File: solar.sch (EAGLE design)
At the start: 13 parts, among them J1 POWERPOLE_POWER10AWG, J2 POWERPOLE_POWER10AWG, J3 POWERPOLE_POWER10AWG, J4 POWERPOLE_POWER10AWG, J5 POWERPOLE_POWER10AWG

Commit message: Uses PCB mount instead of cable for power pole
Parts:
- J1, J2, J3, J4, J5: value POWERPOLE_POWER10AWG -> POWERPOLE_POWER25A; device powerpoles:POWERPOLE_POWER10AWG -> powerpoles:POWERPOLE_POWER25A
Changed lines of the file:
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@@
 </classes>
 <parts>
-<part name="J1" library="powerpoles" deviceset="POWERPOLE_POWER" device="10AWG"/>
-<part name="J2" library="powerpoles" deviceset="POWERPOLE_POWER" device="10AWG"/>
-<part name="J3" library="powerpoles" deviceset="POWERPOLE_POWER" device="10AWG"/>
-<part name="J4" library="powerpoles" deviceset="POWERPOLE_POWER" device="10AWG"/>
-<part name="J5" library="powerpoles" deviceset="POWERPOLE_POWER" device="10AWG"/>
+<part name="J1" library="powerpoles" deviceset="POWERPOLE_POWER" device="25A" value="POWERPOLE_POWER25A"/>
+<part name="J2" library="powerpoles" deviceset="POWERPOLE_POWER" device="25A" value="POWERPOLE_POWER25A"/>
+<part name="J3" library="powerpoles" deviceset="POWERPOLE_POWER" device="25A" value="POWERPOLE_POWER25A"/>
+<part name="J4" library="powerpoles" deviceset="POWERPOLE_POWER" device="25A" value="POWERPOLE_POWER25A"/>
+<part name="J5" library="powerpoles" deviceset="POWERPOLE_POWER" device="25A" value="POWERPOLE_POWER25A"/>
 <part name="GND1" library="glacsweb" deviceset="GND" device=""/>
 <part name="GND2" library="glacsweb" deviceset="GND" device=""/>

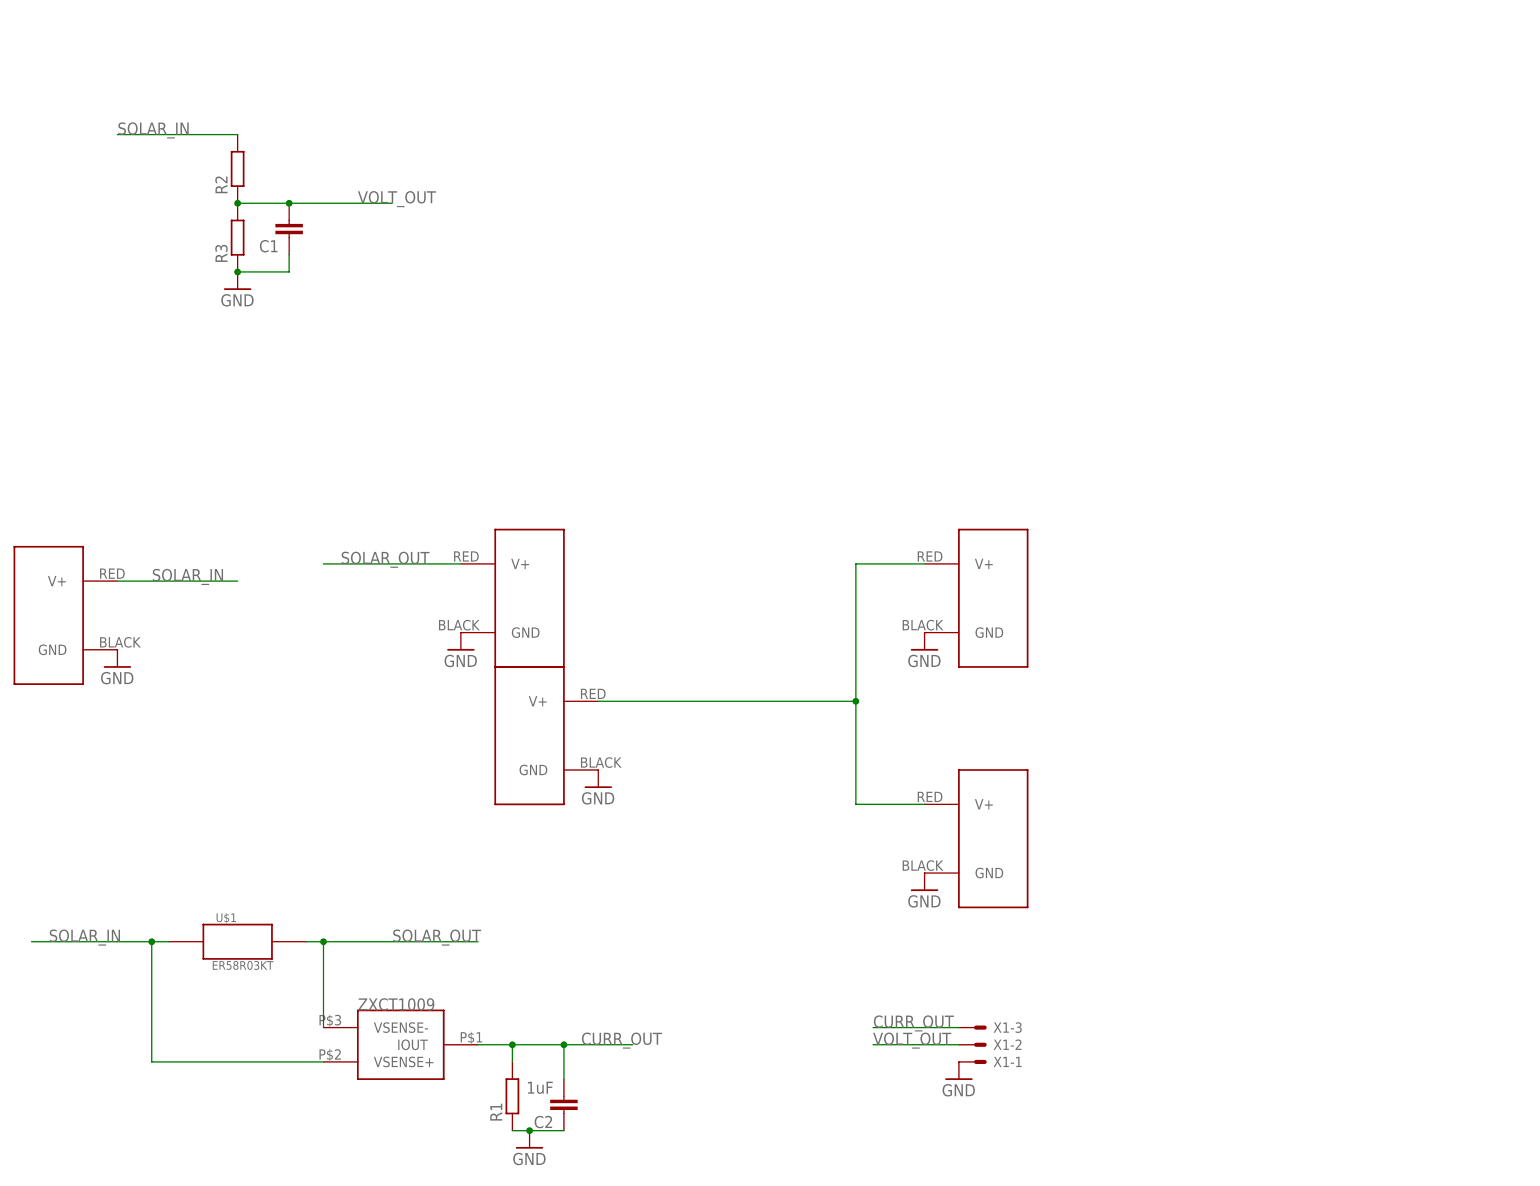
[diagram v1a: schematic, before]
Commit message: now uses smaller frame
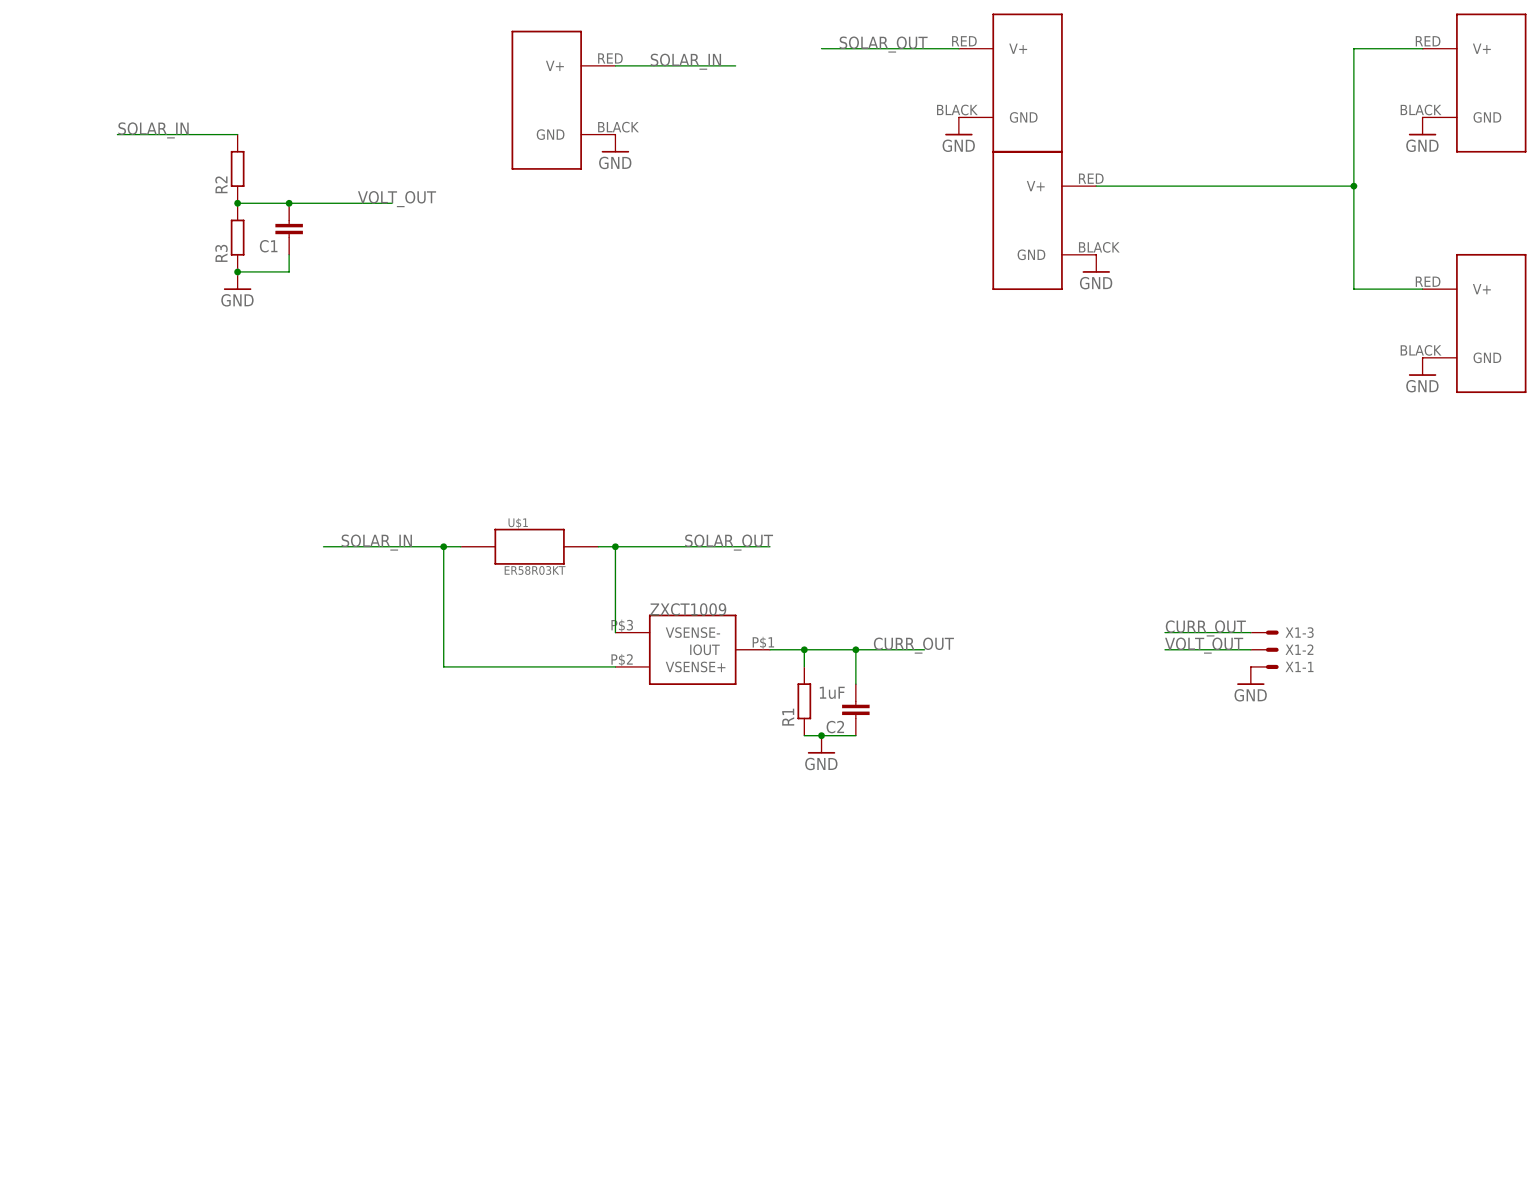
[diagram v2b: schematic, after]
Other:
- moved on the sheet: C2, R1, U$1, X1-1, X1-2, X1-3
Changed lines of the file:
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@@
 <part name="GND8" library="glacsweb" deviceset="GND" device=""/>
 <part name="GND7" library="glacsweb" deviceset="GND" device=""/>
+<part name="FRAME1" library="frames" deviceset="A4L-LOC" device=""/>
 </parts>
 <sheets>
@@
 </plain>
 <instances>
-<instance part="J1" gate="G$1" x="10.16" y="73.66" rot="MR0"/>
-<instance part="J2" gate="G$1" x="81.28" y="55.88" rot="MR0"/>
-<instance part="J3" gate="G$1" x="81.28" y="76.2"/>
-<instance part="J4" gate="G$1" x="149.86" y="76.2"/>
-<instance part="J5" gate="G$1" x="149.86" y="40.64"/>
-<instance part="GND1" gate="1" x="20.32" y="66.04"/>
-<instance part="GND2" gate="1" x="71.12" y="68.58"/>
-<instance part="GND3" gate="1" x="91.44" y="48.26"/>
-<instance part="GND4" gate="1" x="139.7" y="68.58"/>
-<instance part="GND5" gate="1" x="139.7" y="33.02"/>
-<instance part="U$1" gate="G$1" x="38.1" y="25.4"/>
-<instance part="U$2" gate="G$1" x="63.5" y="10.16"/>
-<instance part="R1" gate="G$1" x="78.74" y="2.54" rot="R90"/>
+<instance part="J1" gate="G$1" x="83.82" y="149.86" rot="MR0"/>
+<instance part="J2" gate="G$1" x="154.94" y="132.08" rot="MR0"/>
+<instance part="J3" gate="G$1" x="154.94" y="152.4"/>
+<instance part="J4" gate="G$1" x="223.52" y="152.4"/>
+<instance part="J5" gate="G$1" x="223.52" y="116.84"/>
+<instance part="GND1" gate="1" x="93.98" y="142.24"/>
+<instance part="GND2" gate="1" x="144.78" y="144.78"/>
+<instance part="GND3" gate="1" x="165.1" y="124.46"/>
+<instance part="GND4" gate="1" x="213.36" y="144.78"/>
+<instance part="GND5" gate="1" x="213.36" y="109.22"/>
+<instance part="U$1" gate="G$1" x="81.28" y="83.82"/>
+<instance part="U$2" gate="G$1" x="106.68" y="68.58"/>
+<instance part="R1" gate="G$1" x="121.92" y="60.96" rot="R90"/>
 <instance part="R2" gate="G$1" x="38.1" y="139.7" rot="R90"/>
 <instance part="R3" gate="G$1" x="38.1" y="129.54" rot="R90"/>
 <instance part="C1" gate="G$1" x="45.72" y="129.54" rot="R180"/>
-<instance part="C2" gate="G$1" x="86.36" y="0" rot="R180"/>
-<instance part="X1" gate="-1" x="147.32" y="7.62"/>
-<instance part="X1" gate="-2" x="147.32" y="10.16"/>
-<instance part="X1" gate="-3" x="147.32" y="12.7"/>
-<instance part="GND6" gate="1" x="81.28" y="-5.08"/>
+<instance part="C2" gate="G$1" x="129.54" y="58.42" rot="R180"/>
+<instance part="X1" gate="-1" x="190.5" y="66.04"/>
+<instance part="X1" gate="-2" x="190.5" y="68.58"/>
+<instance part="X1" gate="-3" x="190.5" y="71.12"/>
+<instance part="GND6" gate="1" x="124.46" y="53.34"/>
 <instance part="GND8" gate="1" x="38.1" y="121.92"/>
-<instance part="GND7" gate="1" x="144.78" y="5.08"/>
+<instance part="GND7" gate="1" x="187.96" y="63.5"/>
+<instance part="FRAME1" gate="G$1" x="0" y="0"/>
 </instances>
 <busses>
@@
 <pinref part="R1" gate="G$1" pin="1"/>
 <pinref part="C2" gate="G$1" pin="1"/>
-<wire x1="78.74" y1="-2.54" x2="81.28" y2="-2.54" width="0.1524" layer="91"/>
+<wire x1="121.92" y1="55.88" x2="124.46" y2="55.88" width="0.1524" layer="91"/>
 <pinref part="GND6" gate="1" pin="GND"/>
-<wire x1="81.28" y1="-2.54" x2="86.36" y2="-2.54" width="0.1524" layer="91"/>
-<junction x="81.28" y="-2.54"/>
+<wire x1="124.46" y1="55.88" x2="129.54" y2="55.88" width="0.1524" layer="91"/>
+<junction x="124.46" y="55.88"/>
 </segment>
 <segment>
@@
 <segment>
 <pinref part="J2" gate="G$1" pin="V+"/>
-<wire x1="91.44" y1="60.96" x2="129.54" y2="60.96" width="0.1524" layer="91"/>
-<wire x1="129.54" y1="60.96" x2="129.54" y2="81.28" width="0.1524" layer="91"/>
+<wire x1="165.1" y1="137.16" x2="203.2" y2="137.16" width="0.1524" layer="91"/>
+<wire x1="203.2" y1="137.16" x2="203.2" y2="157.48" width="0.1524" layer="91"/>
 <pinref part="J4" gate="G$1" pin="V+"/>
-<wire x1="129.54" y1="81.28" x2="139.7" y2="81.28" width="0.1524" layer="91"/>
+<wire x1="203.2" y1="157.48" x2="213.36" y2="157.48" width="0.1524" layer="91"/>
 <pinref part="J5" gate="G$1" pin="V+"/>
-<wire x1="139.7" y1="45.72" x2="129.54" y2="45.72" width="0.1524" layer="91"/>
-<wire x1="129.54" y1="45.72" x2="129.54" y2="60.96" width="0.1524" layer="91"/>
-<junction x="129.54" y="60.96"/>
+<wire x1="213.36" y1="121.92" x2="203.2" y2="121.92" width="0.1524" layer="91"/>
+<wire x1="203.2" y1="121.92" x2="203.2" y2="137.16" width="0.1524" layer="91"/>
+<junction x="203.2" y="137.16"/>
 </segment>
 </net>
@@
 <segment>
 <pinref part="J1" gate="G$1" pin="V+"/>
-<wire x1="20.32" y1="78.74" x2="38.1" y2="78.74" width="0.1524" layer="91"/>
-<label x="25.4" y="78.74" size="1.778" layer="95"/>
+<wire x1="93.98" y1="154.94" x2="111.76" y2="154.94" width="0.1524" layer="91"/>
+<label x="99.06" y="154.94" size="1.778" layer="95"/>
 </segment>
 <segment>
 <pinref part="U$1" gate="G$1" pin="P$1"/>
-<wire x1="27.94" y1="25.4" x2="25.4" y2="25.4" width="0.1524" layer="91"/>
-<label x="10.16" y="25.4" size="1.778" layer="95"/>
+<wire x1="71.12" y1="83.82" x2="68.58" y2="83.82" width="0.1524" layer="91"/>
+<label x="53.34" y="83.82" size="1.778" layer="95"/>
 <pinref part="U$2" gate="G$1" pin="VSENSE+"/>
-<wire x1="25.4" y1="25.4" x2="7.62" y2="25.4" width="0.1524" layer="91"/>
-<wire x1="50.8" y1="7.62" x2="25.4" y2="7.62" width="0.1524" layer="91"/>
-<wire x1="25.4" y1="7.62" x2="25.4" y2="25.4" width="0.1524" layer="91"/>
-<junction x="25.4" y="25.4"/>
+<wire x1="68.58" y1="83.82" x2="50.8" y2="83.82" width="0.1524" layer="91"/>
+<wire x1="93.98" y1="66.04" x2="68.58" y2="66.04" width="0.1524" layer="91"/>
+<wire x1="68.58" y1="66.04" x2="68.58" y2="83.82" width="0.1524" layer="91"/>
+<junction x="68.58" y="83.82"/>
 </segment>
 <segment>
@@
 <segment>
 <pinref part="J3" gate="G$1" pin="V+"/>
-<wire x1="71.12" y1="81.28" x2="50.8" y2="81.28" width="0.1524" layer="91"/>
-<label x="53.34" y="81.28" size="1.778" layer="95"/>
+<wire x1="144.78" y1="157.48" x2="124.46" y2="157.48" width="0.1524" layer="91"/>
+<label x="127" y="157.48" size="1.778" layer="95"/>
 </segment>
 <segment>
 <pinref part="U$1" gate="G$1" pin="P$2"/>
-<wire x1="48.26" y1="25.4" x2="50.8" y2="25.4" width="0.1524" layer="91"/>
-<label x="60.96" y="25.4" size="1.778" layer="95"/>
+<wire x1="91.44" y1="83.82" x2="93.98" y2="83.82" width="0.1524" layer="91"/>
+<label x="104.14" y="83.82" size="1.778" layer="95"/>
 <pinref part="U$2" gate="G$1" pin="VSENSE-"/>
-<wire x1="50.8" y1="25.4" x2="73.66" y2="25.4" width="0.1524" layer="91"/>
-<wire x1="50.8" y1="12.7" x2="50.8" y2="25.4" width="0.1524" layer="91"/>
-<junction x="50.8" y="25.4"/>
+<wire x1="93.98" y1="83.82" x2="116.84" y2="83.82" width="0.1524" layer="91"/>
+<wire x1="93.98" y1="71.12" x2="93.98" y2="83.82" width="0.1524" layer="91"/>
+<junction x="93.98" y="83.82"/>
 </segment>
 </net>
@@
 <pinref part="U$2" gate="G$1" pin="IOUT"/>
 <pinref part="R1" gate="G$1" pin="2"/>
-<wire x1="73.66" y1="10.16" x2="78.74" y2="10.16" width="0.1524" layer="91"/>
-<wire x1="78.74" y1="10.16" x2="78.74" y2="7.62" width="0.1524" layer="91"/>
+<wire x1="116.84" y1="68.58" x2="121.92" y2="68.58" width="0.1524" layer="91"/>
+<wire x1="121.92" y1="68.58" x2="121.92" y2="66.04" width="0.1524" layer="91"/>
 <pinref part="C2" gate="G$1" pin="2"/>
-<wire x1="78.74" y1="10.16" x2="86.36" y2="10.16" width="0.1524" layer="91"/>
-<wire x1="86.36" y1="10.16" x2="86.36" y2="5.08" width="0.1524" layer="91"/>
-<wire x1="86.36" y1="10.16" x2="96.52" y2="10.16" width="0.1524" layer="91"/>
-<junction x="78.74" y="10.16"/>
-<junction x="86.36" y="10.16"/>
-<label x="88.9" y="10.16" size="1.778" layer="95"/>
+<wire x1="121.92" y1="68.58" x2="129.54" y2="68.58" width="0.1524" layer="91"/>
+<wire x1="129.54" y1="68.58" x2="129.54" y2="63.5" width="0.1524" layer="91"/>
+<wire x1="129.54" y1="68.58" x2="139.7" y2="68.58" width="0.1524" layer="91"/>
+<junction x="121.92" y="68.58"/>
+<junction x="129.54" y="68.58"/>
+<label x="132.08" y="68.58" size="1.778" layer="95"/>
 </segment>
 <segment>
 <pinref part="X1" gate="-3" pin="S"/>
-<wire x1="144.78" y1="12.7" x2="132.08" y2="12.7" width="0.1524" layer="91"/>
-<label x="132.08" y="12.7" size="1.778" layer="95"/>
+<wire x1="187.96" y1="71.12" x2="175.26" y2="71.12" width="0.1524" layer="91"/>
+<label x="175.26" y="71.12" size="1.778" layer="95"/>
 </segment>
 </net>
@@
 <segment>
 <pinref part="X1" gate="-2" pin="S"/>
-<wire x1="144.78" y1="10.16" x2="132.08" y2="10.16" width="0.1524" layer="91"/>
-<label x="132.08" y="10.16" size="1.778" layer="95"/>
+<wire x1="187.96" y1="68.58" x2="175.26" y2="68.58" width="0.1524" layer="91"/>
+<label x="175.26" y="68.58" size="1.778" layer="95"/>
 </segment>
 </net>
